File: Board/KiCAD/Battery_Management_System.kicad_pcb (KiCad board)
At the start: 4 copper layers, 105 parts, among them J1 Conn_01x06_Socket, J2 Conn_ARM_SWD_TagConnect_TC2030, J4 Conn_01x03, J5 Conn_01x03, J7 Conn_01x05, J8 Conn_01x02, J9 Conn_01x02, Q1 AON7408, Q10 AON7407, Q2 AON7408, Q23 2N7002, Q24 2N7002, Q25 2N7002, Q26 2N7002, Q3 AON7408, Q4 AON7408, Q5 BSS83P, Q6 BSS83P, Q7 BSS83P, Q8 BSS83P, SW2 SW_Push, U1 BQ25730RSNR, U3 LTC2943CDD_PBF, U4 INA260, U5 LMR50410, U6 INA260, U7 INA260, U8 INA260, U9 STM32F103C8T6, Y4 CM8V-T1A-32.768KHZ-12.5PF-20P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, Y5 8MHz

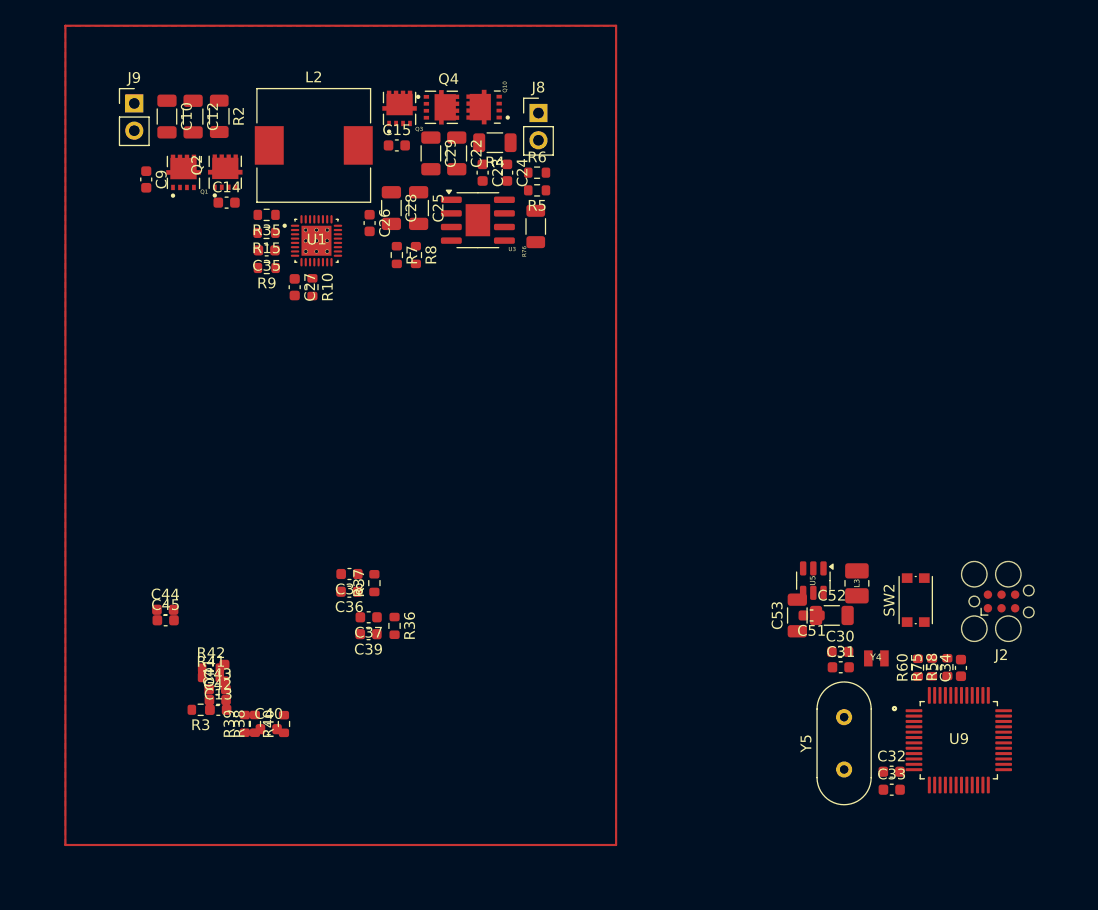
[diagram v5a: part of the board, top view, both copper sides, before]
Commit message: Updated Schematic & PCB Layout
Updated the look of the PCB layout to make the power flow Vin more intuitive.

@KeytarGoblin
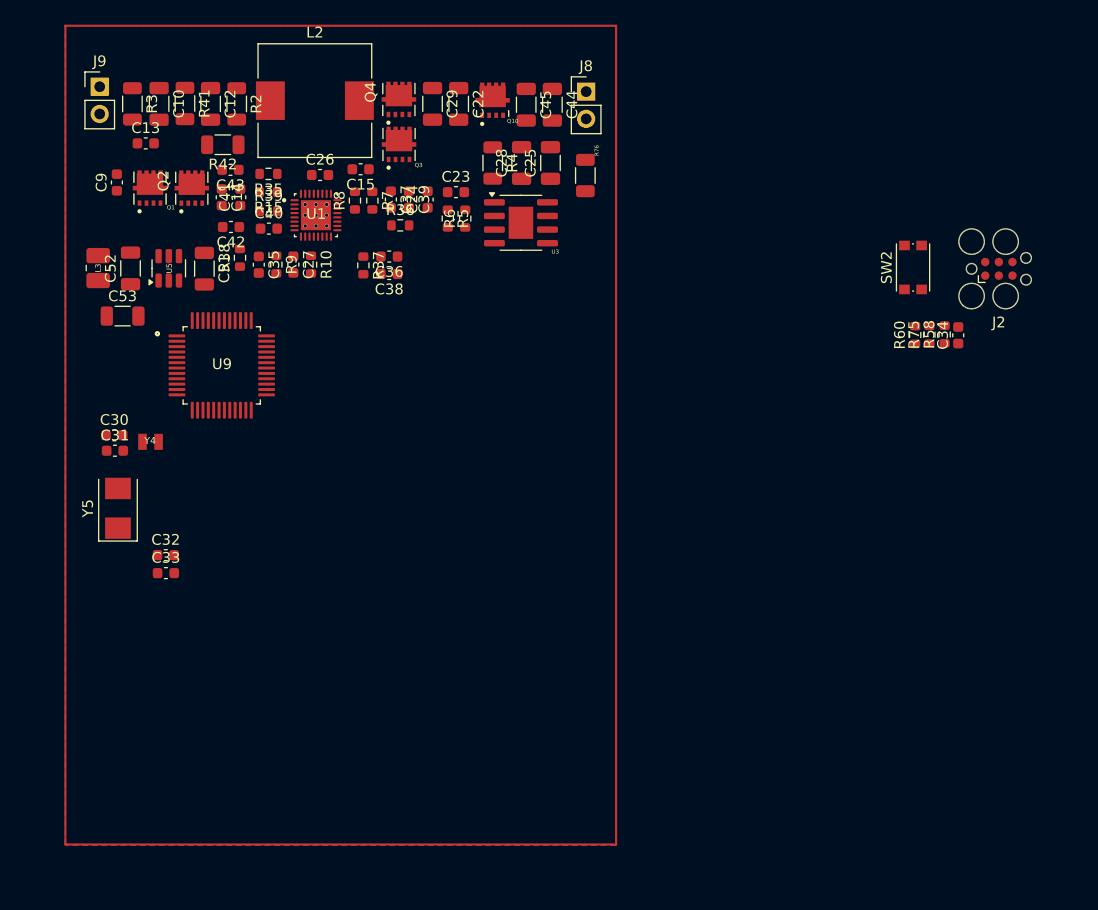
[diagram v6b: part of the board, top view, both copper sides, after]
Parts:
- removed R40: 10, Resistor_SMD:R_0603_1608Metric
- C44, C45, C51: footprint Capacitor_SMD:C_0603_1608Metric -> Capacitor_SMD:C_1206_3216Metric
- R3, R41, R42: footprint Resistor_SMD:R_0603_1608Metric -> Resistor_SMD:R_1206_3216Metric
- Y5: footprint Crystal:Crystal_HC49-4H_Vertical -> Crystal:Crystal_SMD_5032-2Pin_5.0x3.2mm
- moved U9 77.1 mm to (217.7, 78.3)
- moved L3 76.6 mm to (206.2, 69.3), turned to -90 degrees
- moved C52 73.0 mm to (209.2, 69.3), turned to 90 degrees
- moved Y5 72.0 mm to (208.1, 91.7)
- moved Y4 70.6 mm to (211.1, 85.5)
- moved C30 70.6 mm to (207.7, 84.9)
- moved C31 70.6 mm to (207.8, 86.3)
- moved C32 70.6 mm to (212.5, 96.0)
- moved C33 70.6 mm to (212.5, 97.7)
- moved C53 68.8 mm to (208.5, 73.7), turned to 0 degrees
- moved U5 66.8 mm to (212.8, 69.3), turned to 90 degrees
- moved C51 65.2 mm to (216.1, 69.3), turned to -90 degrees
- moved C44 59.3 mm to (248.6, 54.0), turned to -90 degrees
- moved C45 58.7 mm to (246.1, 54.0), turned to -90 degrees
- moved R3 56.9 mm to (209.4, 53.9), turned to -90 degrees
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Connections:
- C40 pad 2: Net-(U1-VDDA) -> VDDA
- R39 pad 2: Net-(U1-VDDA) -> VDDA
- U1 pad 7: Net-(U1-VDDA) -> VDDA

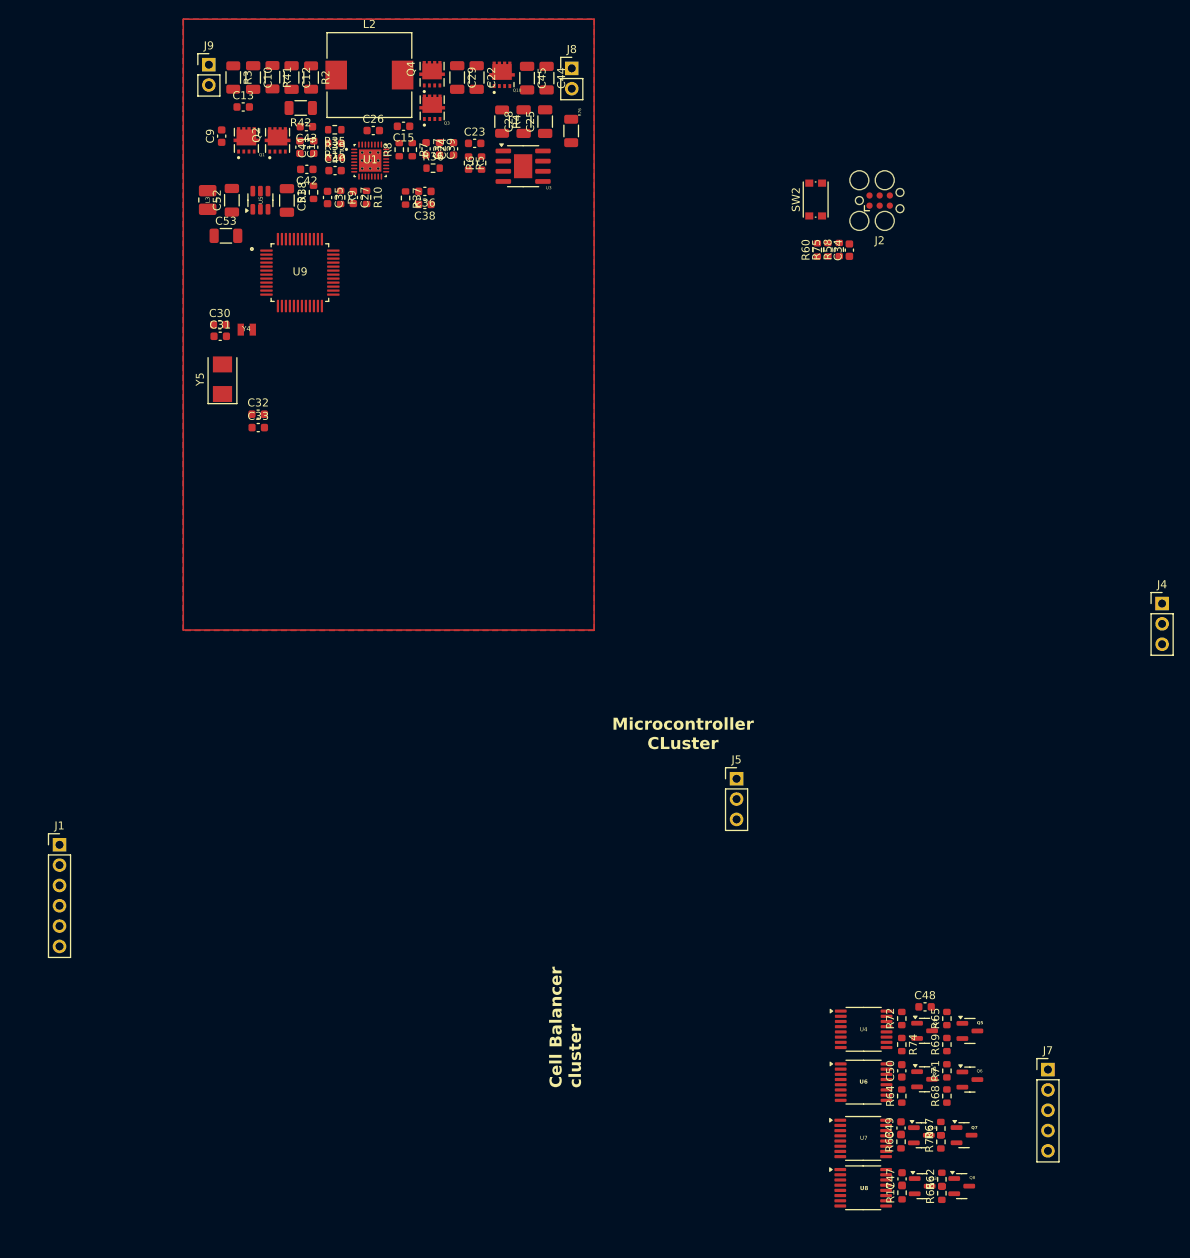
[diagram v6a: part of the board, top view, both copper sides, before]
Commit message: Completed PCB Layout
fully placed all components within the bound of the first iteration of the PCB. We are good to start traceout @KeytarGoblin @andrewgreenberg
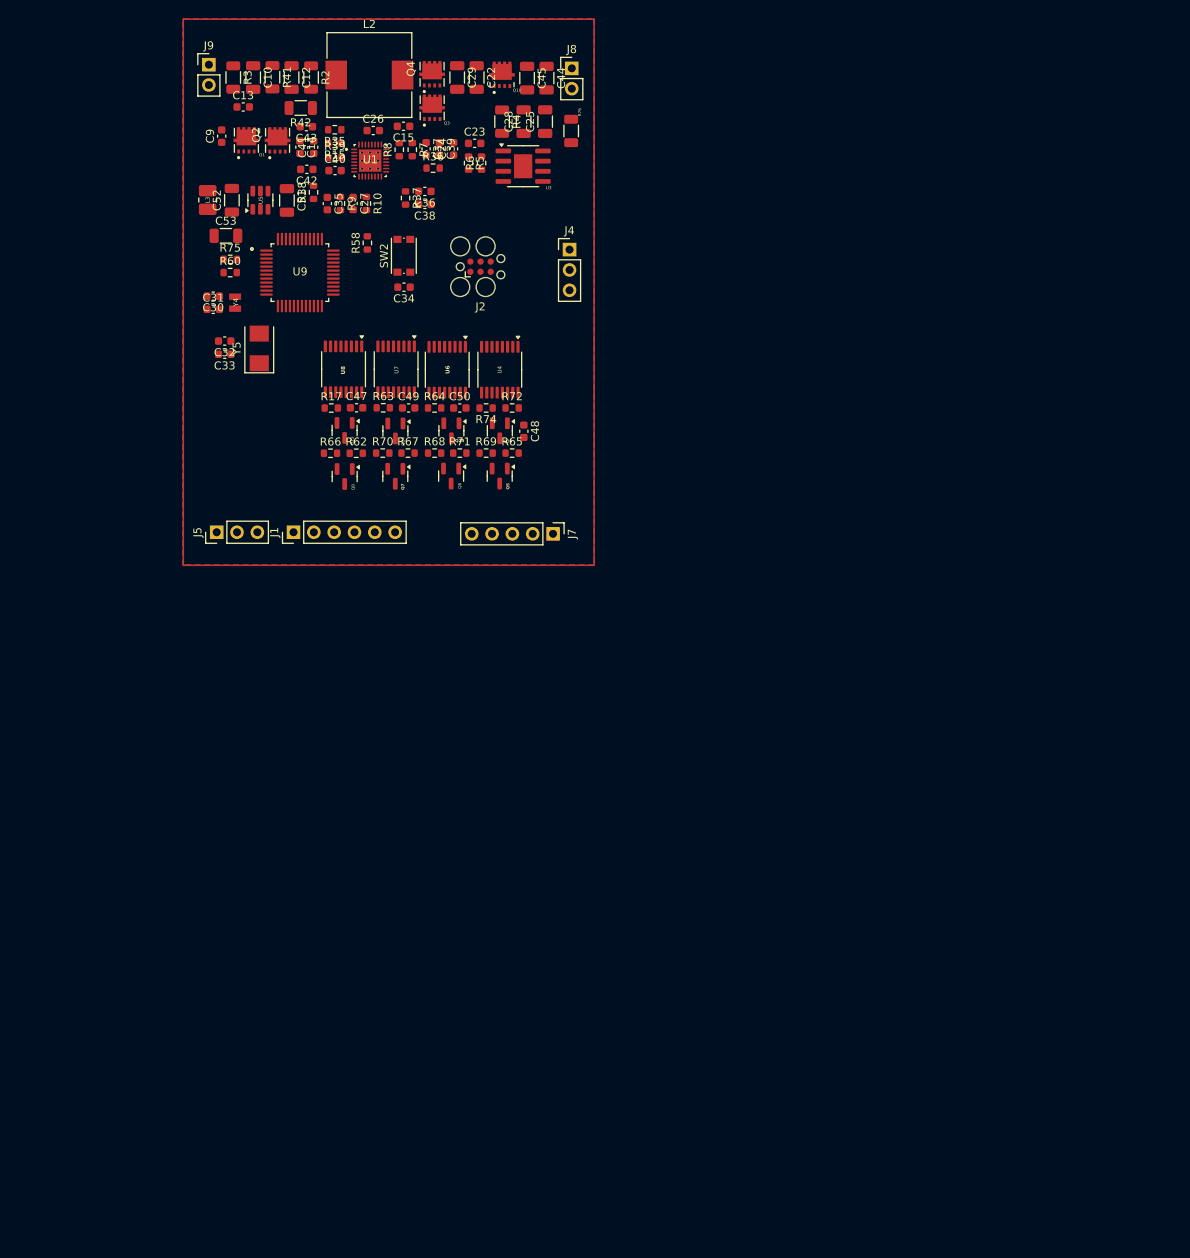
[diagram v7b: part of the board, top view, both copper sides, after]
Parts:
- moved R17 121.3 mm to (221.7, 95.3), turned to 0 degrees
- moved U8 121.2 mm to (223.2, 90.4), turned to -90 degrees
- moved R66 120.0 mm to (221.6, 100.9), turned to 0 degrees
- moved Q23 118.9 mm to (223.3, 98.1), turned to -90 degrees
- moved C47 118.1 mm to (224.8, 95.2), turned to 0 degrees
- moved Q8 117.5 mm to (223.3, 103.8), turned to -90 degrees
- moved R62 116.6 mm to (224.8, 100.9), turned to 0 degrees
- moved U7 112.5 mm to (229.8, 90.4), turned to -90 degrees
- moved R63 112.3 mm to (228.2, 95.2), turned to 0 degrees
- moved R70 110.8 mm to (228.1, 100.9), turned to 0 degrees
- moved Q24 109.9 mm to (229.7, 98.1), turned to -90 degrees
- moved C49 109.0 mm to (231.3, 95.3), turned to 0 degrees
- moved Q7 108.8 mm to (229.7, 103.8), turned to -90 degrees
- moved R67 107.5 mm to (231.2, 100.9), turned to 0 degrees
- moved R64 104.0 mm to (234.6, 95.3), turned to 0 degrees
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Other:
- board text removed: "Cell Balancer cluster"
- board text removed: "Microcontroller CLuster"

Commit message: updated version of PCB
here's my latest update @KeytarGoblin  @andrewgreenberg
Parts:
- R76: value 50m -> 20m
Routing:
- net GND: vias 0 -> 1
- added copper zone on In2.Cu, net /Charge Control/VBus
- added copper zone on In2.Cu, net /Charge Control/Vsys
- added copper zone on In1.Cu, net GND
- removed copper zone on B.Cu, net (none)
- removed copper zone on F.Cu, net (none)
- removed copper zone on In1.Cu, net (none)
- removed copper zone on In2.Cu, net (none)
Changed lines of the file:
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@@
 			(net 67 "unconnected-(U9-PA1-Pad11)")
 			(pinfunction "PA1")
-			(pintype "bidirectional")
+			(pintype "no_connect")
 			(solder_mask_margin 0.102)
 		)
@@
 			(net 91 "unconnected-(U9-PB2-Pad20)")
 			(pinfunction "PB2")
-			(pintype "bidirectional")
+			(pintype "no_connect")
 			(solder_mask_margin 0.102)
 		)
@@
 			(net 74 "unconnected-(U9-PB12-Pad25)")
 			(pinfunction "PB12")
-			(pintype "bidirectional")
+			(pintype "no_connect")
 			(solder_mask_margin 0.102)
 		)
@@
 			(net 83 "unconnected-(U9-PB13-Pad26)")
 			(pinfunction "PB13")
-			(pintype "bidirectional")
+			(pintype "no_connect")
 			(solder_mask_margin 0.102)
 		)
@@
 			(net 88 "unconnected-(U9-PB14-Pad27)")
 			(pinfunction "PB14")
-			(pintype "bidirectional")
+			(pintype "no_connect")
 			(solder_mask_margin 0.102)
 		)
@@
 			(net 82 "unconnected-(U9-PB15-Pad28)")
 			(pinfunction "PB15")
-			(pintype "bidirectional")
+			(pintype "no_connect")
 			(solder_mask_margin 0.102)
 		)
@@
 			(net 69 "unconnected-(U9-PA8-Pad29)")
 			(pinfunction "PA8")
-			(pintype "bidirectional")
+			(pintype "no_connect")
 			(solder_mask_margin 0.102)
 		)
@@
 			(net 80 "unconnected-(U9-PA11-Pad32)")
 			(pinfunction "PA11")
-			(pintype "bidirectional")
+			(pintype "no_connect")
 			(solder_mask_margin 0.102)
 		)
@@
 			(net 90 "unconnected-(U9-PA12-Pad33)")
 			(pinfunction "PA12")
-			(pintype "bidirectional")
+			(pintype "no_connect")
 			(solder_mask_margin 0.102)
 		)
@@
 			(net 87 "unconnected-(U9-PA15-Pad38)")
 			(pinfunction "PA15")
-			(pintype "bidirectional")
+			(pintype "no_connect")
 			(solder_mask_margin 0.102)
 		)
@@
 			(net 81 "unconnected-(U9-PB3-Pad39)")
 			(pinfunction "PB3")
-			(pintype "bidirectional")
+			(pintype "no_connect")
 			(solder_mask_margin 0.102)
 		)
@@
 			(net 79 "unconnected-(U9-PB4-Pad40)")
 			(pinfunction "PB4")
-			(pintype "bidirectional")
+			(pintype "no_connect")
 			(solder_mask_margin 0.102)
 		)
@@
 			(net 75 "unconnected-(U9-PB5-Pad41)")
 			(pinfunction "PB5")
-			(pintype "bidirectional")
+			(pintype "no_connect")
 			(solder_mask_margin 0.102)
 		)
@@
 			(net 77 "unconnected-(U9-PB8-Pad45)")
 			(pinfunction "PB8")
-			(pintype "bidirectional")
+			(pintype "no_connect")
 			(solder_mask_margin 0.102)
 		)
@@
 			(net 71 "unconnected-(U9-PB9-Pad46)")
 			(pinfunction "PB9")
-			(pintype "bidirectional")
+			(pintype "no_connect")
 			(solder_mask_margin 0.102)
 		)
@@
 			)
 		)
-		(property "Value" "50m"
+		(property "Value" "20m"
 			(at 0 1.83 90)
 			(layer "F.Fab")
@@
 		(layer "F.Cu")
 	)
-	(gr_rect
-		(start 50.9524 126.5428)
-		(end 102.3112 202.946)
-		(stroke
-			(width 0.2)
-			(type solid)
-		)
-		(fill no)
-		(layer "B.Cu")
+	(via
+		(at 246.3292 70.5612)
+		(size 0.6)
+		(drill 0.3)
+		(layers "F.Cu" "B.Cu")
+		(free yes)
+		(net 1)
 	)
-	(gr_rect
-		(start 50.9524 126.5428)
-		(end 102.3112 202.946)
-		(stroke
-			(width 0.2)
-			(type solid)
-		)
-		(fill no)
+	(zone
+		(net 1)
+		(net_name "GND")
 		(layer "In1.Cu")
-	)
-	(gr_rect
-		(start 50.9524 126.5428)
-		(end 102.3112 202.946)
-		(stroke
-			(width 0.2)
-			(type solid)
+		(hatch edge 0.5)
+		(connect_pads yes
+			(clearance 0.2)
 		)
-		(fill no)
+		(min_thickness 0.127)
+		(filled_areas_thickness no)
+		(fill yes
+			(thermal_gap 0.127)
+			(thermal_bridge_width 0.5)
+			(smoothing fillet)
+			(radius 0.2)
+			(island_removal_mode 1)
+			(island_area_min 9.999997)
+		)
+		(polygon
+			(pts
+				(xy 203.1492 46.6598) (xy 254.508 46.6598) (xy 254.508 114.923) (xy 203.1492 114.923)
+			)
+		)
+	)
+	(zone
+		(net 2)
+		(net_name "/Charge Control/VBus")
 		(layer "In2.Cu")
+		(hatch edge 0.5)
+		(priority 1)
+		(connect_pads yes
+			(clearance 0.2)
+		)
+		(min_thickness 0.127)
+		(filled_areas_thickness no)
+		(fill yes
+			(thermal_gap 0.127)
+			(thermal_bridge_width 0.5)
+			(smoothing fillet)
+			(radius 0.2)
+			(island_removal_mode 1)
+			(island_area_min 9.999998)
+		)
+		(polygon
+			(pts
+				(xy 203.1492 46.6598) (xy 203.1492 62.3824) (xy 220.091 62.3824) (xy 220.1418 46.6598)
+			)
+		)
 	)
 	(zone
-		(net 0)
-		(net_name "")
-		(layers "F.Cu" "B.Cu" "In1.Cu" "In2.Cu")
+		(net 8)
+		(net_name "/Charge Control/Vsys")
+		(layer "In2.Cu")
 		(hatch edge 0.5)
+		(priority 2)
 		(connect_pads yes
 			(clearance 0.2)
@@
 		(min_thickness 0.127)
 		(filled_areas_thickness no)
-		(fill
+		(fill yes
 			(thermal_gap 0.127)
 			(thermal_bridge_width 0.5)
@@
 		(polygon
 			(pts
-				(xy 203.1492 46.6598) (xy 254.508 46.6598) (xy 254.508 114.923) (xy 203.1492 114.923)
+				(xy 254.508 46.6598) (xy 254.508 54.8386) (xy 232.3846 54.8132) (xy 232.3846 46.5836)
 			)
 		)
